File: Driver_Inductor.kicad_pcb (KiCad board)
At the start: 6 copper layers, 120.6 x 69.9 mm, 84 parts, among them J1 Control_A, J2 DC+, J3 DC-, J4 OUT1, J5 OUT2, U2 R-785.0-1.0, U3 LM1117GS-3.3, U4 LMV7219M5, U5 ADuM1200AR, U6 74LVC1G04

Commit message: Развел все дорожки
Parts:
- removed D15, D16: WRA1215S-3WR2, Mornsun:WRA1215S-3WR2
- removed R32, R33: 0, Resistor_SMD:R_0805_2012Metric_Pad1.20x1.40mm_HandSolder
- removed U2: R-785.0-1.0, Converter_DCDC:Converter_DCDC_RECOM_R-78E-0.5_THT
- added C10: 1u, Capacitor_THT:C_Rect_L31.5mm_W13.0mm_P27.50mm_MKS4, F.Cu at (87.0, 83.2)
- added C9: 2.2u, Capacitor_SMD:C_0805_2012Metric_Pad1.18x1.45mm_HandSolder, B.Cu at (132.7, 87.6)
- added D11: WRA1215S-3WR2, Mornsun:WRA_S-3WR2, F.Cu at (151.5, 99.1)
- added D12: K78xxM-1000R3, Mornsun:K78xx-1000R3, F.Cu at (177.8, 109.7)
- added D6: SN74AHC1G08DBVR, Package_TO_SOT_SMD:SOT-23-5, F.Cu at (126.7, 83.3)
- added D8: WRA1215S-3WR2, Mornsun:WRA_S-3WR2, F.Cu at (118.5, 99.1)
- C1, C17, C18, C2, C20, C22, C23, C24, C25, C26, C28, C3, C30, C33, C37, C4, D17, R14, R31, U6: moved to F.Cu
- C15, C8: moved to B.Cu
- J2, J3, J4, J5: footprint Connector_Power:M5 -> Connector_My:Bush_M4
- moved C30 102.9 mm to (158.1, 106.4), turned to 0 degrees
- moved J4 93.4 mm to (120.0, 68.0)
- moved C17 73.4 mm to (152.4, 85.1), turned to 90 degrees
- moved C16 69.8 mm to (166.5, 75.0), turned to 180 degrees
- moved C18 66.7 mm to (119.4, 85.1), turned to 90 degrees
- moved J5 64.8 mm to (139.5, 68.0)
- moved C31 62.5 mm to (173.5, 68.0), turned to -90 degrees
- moved C34 61.5 mm to (183.5, 71.5)
- moved C35 61.5 mm to (183.5, 76.5)
- moved C33 58.4 mm to (176.5, 68.0), turned to 90 degrees
- moved C24 50.1 mm to (124.5, 108.0), turned to 0 degrees
- moved C23 49.7 mm to (129.5, 108.0)
- moved C36 48.5 mm to (189.0, 76.5), turned to 180 degrees
- moved C26 45.4 mm to (135.9, 108.0)
- moved C25 45.4 mm to (141.0, 108.0), turned to 180 degrees
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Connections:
- net DESAT_H renamed DC+
- net Net-(J3-Pin_1) renamed DC-
- C23 pad 1: +15V_L1 -> -15V_L
- C24 pad 2: -15V_L1 -> +15V_L
- C25 pad 1: +15V_H1 -> -15V_H
- C26 pad 2: -15V_H1 -> +15V_H
- C30 pad 1: E2 -> E3
- C30 pad 2: -15V_L1 -> -15V_H
- C31 pad 2: -15V_L1 -> -15V_H
- C32 pad 2: -15V_L1 -> -15V_H
- C34 pad 2: -15V_L1 -> -15V_H
- D1 pad 13: +15V_L1 -> +15V_L
- D1 pad 16: -15V_L1 -> -15V_L
- D1 pad 9: -15V_L1 -> -15V_L
- D17 pad 1: OUT2 -> OUT2_Sens
- D17 pad 2: OUT2 -> OUT2_Sens
- D17 pad 3: OUT2 -> OUT2_Sens
- D17 pad 4: OUT2 -> OUT2_Sens
- D17 pad 5: OUT2_Sens -> OUT2
- D17 pad 6: OUT2_Sens -> OUT2
- D17 pad 7: OUT2_Sens -> OUT2
- D17 pad 8: OUT2_Sens -> OUT2
- D2 pad 13: +15V_H1 -> +15V_H
- D2 pad 16: -15V_H1 -> -15V_H
- D2 pad 9: -15V_H1 -> -15V_H
- J1 pad 1: unconnected-(J1-Pin_1-Pad1) -> Temp_N
- J1 pad 10: unconnected-(J1-Pin_10-Pad10) -> Fault_N
- J1 pad 11: unconnected-(J1-Pin_11-Pad11) -> PWM2_N
- J1 pad 12: unconnected-(J1-Pin_12-Pad12) -> Current
- J1 pad 2: unconnected-(J1-Pin_2-Pad2) -> +15V
- J1 pad 3: unconnected-(J1-Pin_3-Pad3) -> PWM1_P
- J1 pad 4: unconnected-(J1-Pin_4-Pad4) -> Fault_P
- J1 pad 5: unconnected-(J1-Pin_5-Pad5) -> PWM2_P
- J1 pad 6: unconnected-(J1-Pin_6-Pad6) -> Reset
- J1 pad 7: unconnected-(J1-Pin_7-Pad7) -> Temp_P
- J1 pad 8: unconnected-(J1-Pin_8-Pad8) -> GND
- J1 pad 9: unconnected-(J1-Pin_9-Pad9) -> PWM1_N
- R13 pad 2: unconnected-(R13-Pad2) -> +5V
- R26 pad 1: -15V_L1 -> -15V_H
- U3 pad 1: -15V_L1 -> -15V_H
- U3 pad 3: E2 -> E3
- U4 pad 2: -15V_L1 -> -15V_H
- U5 pad 4: -15V_L1 -> -15V_H
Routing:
- net RDY: track 0.04 -> 54.0 mm, vias 0 -> 5
- net FLT: track 1.02 -> 54.3 mm, vias 0 -> 4
- net Net-(D14-DI): track 0.00 -> 53.0 mm, vias 0 -> 2
- net PWM2_N: track 0.00 -> 48.9 mm, vias 0 -> 1
- net PWM2_P: track 0.00 -> 45.2 mm, vias 0 -> 1
- net Net-(D1-DESAT): track 0.00 -> 45.1 mm, vias 0 -> 2
- net PWM1_N: track 0.00 -> 42.6 mm, vias 0 -> 1
- net +5V: track 0.00 -> 41.6 mm, vias 0 -> 12
- net PWM1_P: track 0.00 -> 38.7 mm, vias 0 -> 1
- net Net-(D2-DESAT): track 0.00 -> 32.7 mm, vias 0 -> 2
- net Reset: track 0.00 -> 31.8 mm, vias 0 -> 1
- net GND: track 0.00 -> 28.3 mm, vias 1 -> 21
- net Current: track 0.09 -> 25.4 mm
- net Temp_N: track 0.00 -> 24.8 mm
- net Temp_P: track 0.00 -> 20.6 mm
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- added copper zone on F.Cu, net +15V
- added copper zone on In4.Cu, net +15V
- added copper zone on In3.Cu, net +15V_H
- added copper zone on In3.Cu, net +15V_L
- added copper zone on F.Cu, net +5V
- added copper zone on In2.Cu, net +5V
- added copper zone on In3.Cu, net +5V
- added copper zone on F.Cu, net +5VP
- added copper zone on In2.Cu, net +5VP
- added copper zone on F.Cu, net -15V_H
- added copper zone on In1.Cu, net -15V_H
- added copper zone on In4.Cu, net -15V_H
- added copper zone on In4.Cu, net -15V_L
- added copper zone on B.Cu, net DC+
- added copper zone on F.Cu, net DC+
- added copper zone on In1.Cu, net DC+
- added copper zone on In2.Cu, net DC+
- added copper zone on In3.Cu, net DC+
- added copper zone on In4.Cu, net DC+
- added copper zone on B.Cu, net DC-
- added copper zone on F.Cu, net DC-
- added copper zone on In1.Cu, net DC-
- added copper zone on In2.Cu, net DC-
- added copper zone on In3.Cu, net DC-
- added copper zone on In4.Cu, net DC-
- added copper zone on B.Cu, net E2
- added copper zone on B.Cu, net E3
- added copper zone on F.Cu, net E3
- added copper zone on F.Cu, net G2
- added copper zone on F.Cu, net G3
- added copper zone on B.Cu, net GND
- added copper zone on F.Cu, net GND
- added copper zone on F.Cu, net Net-(D1-Vout_off)
- added copper zone on F.Cu, net Net-(D1-Vout_on)
- added copper zone on F.Cu, net Net-(D2-Vout_off)
- added copper zone on F.Cu, net Net-(D2-Vout_on)
- added copper zone on B.Cu, net OUT1
- added copper zone on F.Cu, net OUT1
- added copper zone on In1.Cu, net OUT1
- added copper zone on In2.Cu, net OUT1
- added copper zone on In3.Cu, net OUT1
- added copper zone on In4.Cu, net OUT1
- added copper zone on B.Cu, net OUT2
- added copper zone on F.Cu, net OUT2
- added copper zone on In1.Cu, net OUT2
- added copper zone on In2.Cu, net OUT2
- added copper zone on In3.Cu, net OUT2
- added copper zone on In4.Cu, net OUT2
- added copper zone on B.Cu, net OUT2_Sens
- added copper zone on F.Cu, net OUT2_Sens
- added copper zone on In1.Cu, net OUT2_Sens
- added copper zone on In2.Cu, net OUT2_Sens
- added copper zone on In3.Cu, net OUT2_Sens
- added copper zone on In4.Cu, net OUT2_Sens
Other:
- board size 120.6 x 69.9 mm -> 119.6 x 60.5 mm
- board text removed: "Driver GD50FFY120C5S VER1.0.TEST"

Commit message: Заменил в схеме символы питания
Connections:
- net DC+ renamed DESAT_H
- net DC- renamed -VDC
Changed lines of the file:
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@@
 	(net 50 "unconnected-(D20-DC--Pad13)")
 	(net 51 "unconnected-(D20-DC--Pad14)")
-	(net 52 "DC+")
+	(net 52 "-VDC")
 	(net 53 "OUT1")
 	(net 54 "unconnected-(D20-DC+-Pad15)")
@@
 	(net 56 "unconnected-(D20-OUT3-Pad19)")
 	(net 57 "unconnected-(D20-OUT3-Pad20)")
-	(net 58 "DC-")
+	(net 58 "DESAT_H")
 	(net 59 "unconnected-(U5-VOB-Pad6)")
 	(net 60 "unconnected-(U5-VIB-Pad3)")
@@
 		)
 		(fp_text user "${REFERENCE}"
-			(at 0 0 360)
+			(at 0 0 0)
 			(layer "F.Fab")
 			(effects
@@
 		)
 		(property "Value" "120"
-			(at 0 1.65 360)
+			(at 0 1.65 0)
 			(layer "F.Fab")
 			(effects
@@
 		)
 		(property "Footprint" "Resistor_SMD:R_0805_2012Metric_Pad1.20x1.40mm_HandSolder"
-			(at 0 0 360)
+			(at 0 0 0)
 			(layer "F.Fab")
 			(hide yes)
@@
 		)
 		(property "Datasheet" ""
-			(at 0 0 360)
+			(at 0 0 0)
 			(layer "F.Fab")
 			(hide yes)
@@
 		)
 		(property "Description" ""
-			(at 0 0 360)
+			(at 0 0 0)
 			(layer "F.Fab")
 			(hide yes)
@@
 		)
 		(fp_text user "${REFERENCE}"
-			(at 0 0 360)
+			(at 0 0 0)
 			(layer "F.Fab")
 			(effects
@@
 		(tags "SOIC SO")
 		(property "Reference" "D17"
-			(at 3 -6 360)
+			(at 3 -6 0)
 			(layer "F.SilkS")
 			(effects
@@
 		)
 		(property "Value" "NSM2011-50B5R-DSWR"
-			(at 0 6.1 360)
+			(at 0 6.1 0)
 			(layer "F.Fab")
 			(effects
@@
 		)
 		(property "Footprint" "Package_SO:SOIC-16W_7.5x10.3mm_P1.27mm"
-			(at 0 0 360)
+			(at 0 0 0)
 			(layer "B.Fab")
 			(hide yes)
@@
 		)
 		(property "Datasheet" ""
-			(at 0 0 360)
+			(at 0 0 0)
 			(layer "B.Fab")
 			(hide yes)
@@
 		)
 		(property "Description" ""
-			(at 0 0 360)
+			(at 0 0 0)
 			(layer "B.Fab")
 			(hide yes)
@@
 		)
 		(fp_text user "${REFERENCE}"
-			(at 0 0 360)
+			(at 0 0 0)
 			(layer "F.Fab")
 			(effects
@@
 			(layers "*.Cu" "*.Mask")
 			(remove_unused_layers no)
-			(net 52 "DC+")
+			(net 58 "DESAT_H")
 			(pintype "passive")
 		)
@@
 			(layers "*.Cu" "*.Mask")
 			(remove_unused_layers no)
-			(net 58 "DC-")
+			(net 52 "-VDC")
 			(pintype "passive")
 		)
@@
 		)
 		(property "Value" "10k"
-			(at 0 1.65 360)
+			(at 0 1.65 0)
 			(layer "F.Fab")
 			(effects
@@
 		)
 		(property "Footprint" "Resistor_SMD:R_0805_2012Metric_Pad1.20x1.40mm_HandSolder"
-			(at 0 0 360)
+			(at 0 0 0)
 			(layer "F.Fab")
 			(hide yes)
@@
 		)
 		(property "Datasheet" ""
-			(at 0 0 360)
+			(at 0 0 0)
 			(layer "F.Fab")
 			(hide yes)
@@
 		)
 		(property "Description" ""
-			(at 0 0 360)
+			(at 0 0 0)
 			(layer "F.Fab")
 			(hide yes)
@@
 		)
 		(fp_text user "${REFERENCE}"
-			(at 0 0 360)
+			(at 0 0 0)
 			(layer "F.Fab")
 			(effects
@@
 			(layers "F.Cu" "F.Paste" "F.Mask")
 			(roundrect_rratio 0.1388888889)
-			(net 52 "DC+")
+			(net 58 "DESAT_H")
 			(pinfunction "K")
 			(pintype "passive")
@@
 		(tags "capacitor handsolder")
 		(property "Reference" "C30"
-			(at 0 -1.68 360)
+			(at 0 -1.68 0)
 			(layer "F.SilkS")
 			(effects
@@
 		)
 		(property "Value" "2.2u"
-			(at 0 1.68 360)
+			(at 0 1.68 0)
 			(layer "F.Fab")
 			(effects
@@
 		)
 		(property "Footprint" "Capacitor_SMD:C_0805_2012Metric_Pad1.18x1.45mm_HandSolder"
-			(at 0 0 360)
+			(at 0 0 0)
 			(layer "B.Fab")
 			(hide yes)
@@
 		)
 		(property "Datasheet" ""
-			(at 0 0 360)
+			(at 0 0 0)
 			(layer "B.Fab")
 			(hide yes)
@@
 		)
 		(property "Description" ""
-			(at 0 0 360)
+			(at 0 0 0)
 			(layer "B.Fab")
 			(hide yes)
@@
 		)
 		(fp_text user "${REFERENCE}"
-			(at 0 0 360)
+			(at 0 0 0)
 			(layer "F.Fab")
 			(effects
@@
 			(layers "*.Cu" "*.Mask")
 			(remove_unused_layers no)
-			(net 52 "DC+")
+			(net 58 "DESAT_H")
 			(pinfunction "DC+")
 			(pintype "input")
@@
 			(layers "*.Cu" "*.Mask")
 			(remove_unused_layers no)
-			(net 52 "DC+")
+			(net 58 "DESAT_H")
 			(pinfunction "DC+")
 			(pintype "input")
@@
 			(layers "*.Cu" "*.Mask")
 			(remove_unused_layers no)
-			(net 58 "DC-")
+			(net 52 "-VDC")
 			(pinfunction "DC-")
 			(pintype "input")
@@
 			(layers "*.Cu" "*.Mask")
 			(remove_unused_layers no)
-			(net 58 "DC-")
+			(net 52 "-VDC")
 			(pinfunction "DC-")
 			(pintype "input")
@@
 			(layers "*.Cu" "*.Mask")
 			(remove_unused_layers no)
-			(net 52 "DC+")
+			(net 58 "DESAT_H")
 			(pinfunction "Pin_1")
 			(pintype "passive")
@@
 		(tags "connector Molex Micro-Fit_3.0 vertical")
 		(property "Reference" "J1"
-			(at 7.5 -3.67 360)
+			(at 7.5 -3.67 0)
 			(layer "F.SilkS")
 			(effects
@@
 		)
 		(property "Value" "Control_A"
-			(at 7.5 7.51 360)
+			(at 7.5 7.51 0)
 			(layer "F.Fab")
 			(effects
@@
 		)
 		(fp_text user "${REFERENCE}"
-			(at 7.5 4.2 360)
+			(at 7.5 4.2 0)
 			(layer "F.Fab")
 			(effects
@@
 			(layers "*.Cu" "*.Mask")
 			(remove_unused_layers no)
-			(net 58 "DC-")
+			(net 52 "-VDC")
 			(pinfunction "Pin_1")
 			(pintype "passive")
@@
 		(tags "capacitor handsolder")
 		(property "Reference" "C27"
-			(at 2.921 -0.254 360)
+			(at 2.921 -0.254 0)
 			(layer "B.SilkS")
 			(effects
@@
 	)
 	(segment
-		(start 107.315 91.525)
-		(end 105.452 89.662)
+		(start 117.974 76.74)
+		(end 118.382 76.332)
 		(width 0.5)
 		(layer "F.Cu")
-		(net 52)
+		(net 53)
 	)
 	(segment
-		(start 107.315 95.155)
-		(end 107.315 91.525)
+		(start 113.03 76.74)
+		(end 117.974 76.74)
 		(width 0.5)
 		(layer "F.Cu")
-		(net 52)
+		(net 53)
 	)
 	(segment
-		(start 117.974 76.74)
-		(end 118.382 76.332)
+		(start 107.315 91.525)
+		(end 105.452 89.662)
 		(width 0.5)
 		(layer "F.Cu")
-		(net 53)
+		(net 58)
 	)
 	(segment
-		(start 113.03 76.74)
-		(end 117.974 76.74)
+		(start 107.315 95.155)
+		(end 107.315 91.525)
 		(width 0.5)
 		(layer "F.Cu")
-		(net 53)
+		(net 58)
 	)
 	(segment
@@
 		(polygon
 			(pts
-				(xy 167.894 112.522) (xy 168.656 112.522) (xy 168.656 112.522) (xy 173.482 112.522) (xy 173.482 111.252)
-				(xy 177.038 111.252) (xy 177.038 115.062) (xy 167.894 115.062)
+				(xy 167.894 112.522) (xy 168.656 112.522) (xy 173.482 112.522) (xy 173.482 111.252) (xy 177.038 111.252)
+				(xy 177.038 115.062) (xy 167.894 115.062)
 			)
 		)
@@
 		(polygon
 			(pts
-				(xy 167.894 107.95) (xy 167.894 107.95) (xy 167.894 107.442) (xy 172.974 107.442) (xy 172.974 108.458)
-				(xy 177.038 108.458) (xy 177.038 110.998) (xy 172.974 110.998) (xy 172.974 112.268) (xy 167.894 112.268)
-				(xy 167.894 111.506) (xy 167.894 111.506)
+				(xy 167.894 107.95) (xy 167.894 107.442) (xy 172.974 107.442) (xy 172.974 108.458) (xy 177.038 108.458)
+				(xy 177.038 110.998) (xy 172.974 110.998) (xy 172.974 112.268) (xy 167.894 112.268) (xy 167.894 111.506)
 			)
 		)
@@
 	)
 	(zone
-		(net 58)
-		(net_name "DC-")
+		(net 52)
+		(net_name "-VDC")
 		(layers "F.Cu" "In1.Cu" "In2.Cu" "In3.Cu" "In4.Cu" "B.Cu")
 		(hatch edge 0.5)
@@
 	)
 	(zone
-		(net 52)
-		(net_name "DC+")
+		(net 58)
+		(net_name "DESAT_H")
 		(layers "F.Cu" "In1.Cu" "In2.Cu" "In3.Cu" "In4.Cu" "B.Cu")
 		(hatch edge 0.5)
@@
 		(polygon
 			(pts
-				(xy 161.544 104.394) (xy 153.67 104.394) (xy 153.67 104.394) (xy 132.842 104.394) (xy 132.842 110.49)
-				(xy 161.544 110.49)
+				(xy 161.544 104.394) (xy 153.67 104.394) (xy 132.842 104.394) (xy 132.842 110.49) (xy 161.544 110.49)
 			)
 		)
@@
 		(polygon
 			(pts
-				(xy 132.842 104.394) (xy 153.67 104.394) (xy 153.67 104.394) (xy 155.956 104.394) (xy 155.956 110.744)
-				(xy 152.908 110.744) (xy 152.908 119.888) (xy 132.842 119.888)
+				(xy 132.842 104.394) (xy 153.67 104.394) (xy 155.956 104.394) (xy 155.956 110.744) (xy 152.908 110.744)
+				(xy 152.908 119.888) (xy 132.842 119.888)
 			)
 		)

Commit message: VER2.0 Отправил в резонит
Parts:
- removed C37: 56p, Capacitor_SMD:C_0805_2012Metric_Pad1.18x1.45mm_HandSolder
- removed C9: 2.2u, Capacitor_SMD:C_0805_2012Metric_Pad1.18x1.45mm_HandSolder
- removed R30: 120, Resistor_SMD:R_0805_2012Metric_Pad1.20x1.40mm_HandSolder
- removed R31: 10k, Resistor_SMD:R_0805_2012Metric_Pad1.20x1.40mm_HandSolder
- removed U6: 74LVC1G04, Package_TO_SOT_SMD:SOT-23-5_HandSoldering
- added G***: LOGO, Logo:Logo_EV_Tech, F.Cu at (90.6, 67.2)
- added G***: LOGO, Logo:Logo_Megawatt, F.Cu at (192.0, 111.6)
- added Q1: IRLML2402TRPBF, Package_TO_SOT_SMD:SOT-23, F.Cu at (132.8, 83.2)
- added R24: 0, Resistor_SMD:R_0805_2012Metric_Pad1.20x1.40mm_HandSolder, F.Cu at (132.8, 80.4)
- added R32: 1k, Resistor_SMD:R_0805_2012Metric_Pad1.20x1.40mm_HandSolder, F.Cu at (132.8, 86.0)
- D1, D2: value ADUM4135 -> NSI6651ASC-DSWR
- turned D1 to 90 degrees
- turned D2 to 90 degrees
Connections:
- C3 pad 2: Net-(D1-~{RESET}) -> Net-(D1-~{RST})
- C4 pad 2: Net-(D2-~{RESET}) -> Net-(D2-~{RST})
- D1 pad 1: GND -> -15V_L
- D1 pad 10: Net-(D1-DESAT) -> PWM2_P
- D1 pad 11: E2 -> PWM2_N
- D1 pad 12: Net-(D1-Vout_off) -> RDY
- D1 pad 13: +15V_L -> FLT
- D1 pad 14: Net-(D1-Vout_on) -> Net-(D1-~{RST})
- D1 pad 15: G2 -> +5V
- D1 pad 16: -15V_L -> GND
- D1 pad 2: PWM2_P -> Net-(D1-DESAT)
- D1 pad 3: PWM2_N -> E2
- D1 pad 4: RDY -> Net-(D1-OUTH)
- D1 pad 5: FLT -> +15V_L
- D1 pad 6: Net-(D1-~{RESET}) -> Net-(D1-OUTL)
- D1 pad 7: +5V -> G2
- D1 pad 8: GND -> -15V_L
- D1 pad 9: -15V_L -> GND
- D2 pad 1: GND -> -15V_H
- D2 pad 10: Net-(D2-DESAT) -> PWM1_P
- D2 pad 11: E3 -> PWM1_N
- D2 pad 12: Net-(D2-Vout_off) -> RDY
- D2 pad 13: +15V_H -> FLT
- D2 pad 14: Net-(D2-Vout_on) -> Net-(D2-~{RST})
- D2 pad 15: G3 -> +5V
- D2 pad 16: -15V_H -> GND
- D2 pad 2: PWM1_P -> Net-(D2-DESAT)
- D2 pad 3: PWM1_N -> E3
- D2 pad 4: RDY -> Net-(D2-OUTH)
- D2 pad 5: FLT -> +15V_H
- D2 pad 6: Net-(D2-~{RESET}) -> Net-(D2-OUTL)
- D2 pad 7: +5V -> G3
- D2 pad 8: GND -> -15V_H
- D2 pad 9: -15V_H -> GND
- R1 pad 2: Net-(D1-~{RESET}) -> Net-(D1-~{RST})
- R15 pad 2: Net-(D1-Vout_on) -> Net-(D1-OUTL)
- R16 pad 2: Net-(D1-Vout_on) -> Net-(D1-OUTL)
- R17 pad 2: Net-(D1-Vout_off) -> Net-(D1-OUTH)
- R18 pad 2: Net-(D1-Vout_off) -> Net-(D1-OUTH)
- R19 pad 2: Net-(D2-Vout_on) -> Net-(D2-OUTL)
- R2 pad 2: Net-(D2-~{RESET}) -> Net-(D2-~{RST})
- R20 pad 2: Net-(D2-Vout_off) -> Net-(D2-OUTH)
- R21 pad 2: Net-(D2-Vout_off) -> Net-(D2-OUTH)
- R22 pad 2: Net-(D2-Vout_off) -> Net-(D2-OUTH)
- R3 pad 2: Net-(D1-Vout_on) -> Net-(D1-OUTL)
- R4 pad 2: Net-(D1-Vout_off) -> Net-(D1-OUTH)
- R5 pad 2: Net-(D2-Vout_on) -> Net-(D2-OUTL)
- R6 pad 2: Net-(D2-Vout_on) -> Net-(D2-OUTL)
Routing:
- net Net-(C37-Pad1): track 7.17 -> 0.00 mm
- net Net-(D2-~{RST}): track 0.00 -> 6.28 mm
- net Net-(D2-~{RESET}): track 6.28 -> 0.00 mm
- net Net-(D1-~{RST}): track 0.00 -> 6.28 mm
- net Net-(D1-~{RESET}): track 6.28 -> 0.00 mm
- net RST: track 12.7 -> 17.0 mm
- net Net-(Q1-G): track 0.00 -> 1.88 mm
- net +5V: track 41.6 -> 40.0 mm
- net GND: track 28.3 -> 29.1 mm, vias 21 -> 18
- added copper zone on F.Cu, net Net-(D1-OUTH)
- added copper zone on F.Cu, net Net-(D1-OUTL)
- added copper zone on F.Cu, net Net-(D2-OUTH)
- added copper zone on F.Cu, net Net-(D2-OUTL)
- removed copper zone on F.Cu, net Net-(D1-Vout_off)
- removed copper zone on F.Cu, net Net-(D1-Vout_on)
- removed copper zone on F.Cu, net Net-(D2-Vout_off)
- removed copper zone on F.Cu, net Net-(D2-Vout_on)
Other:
- board text added: "Driver board VER2.0"

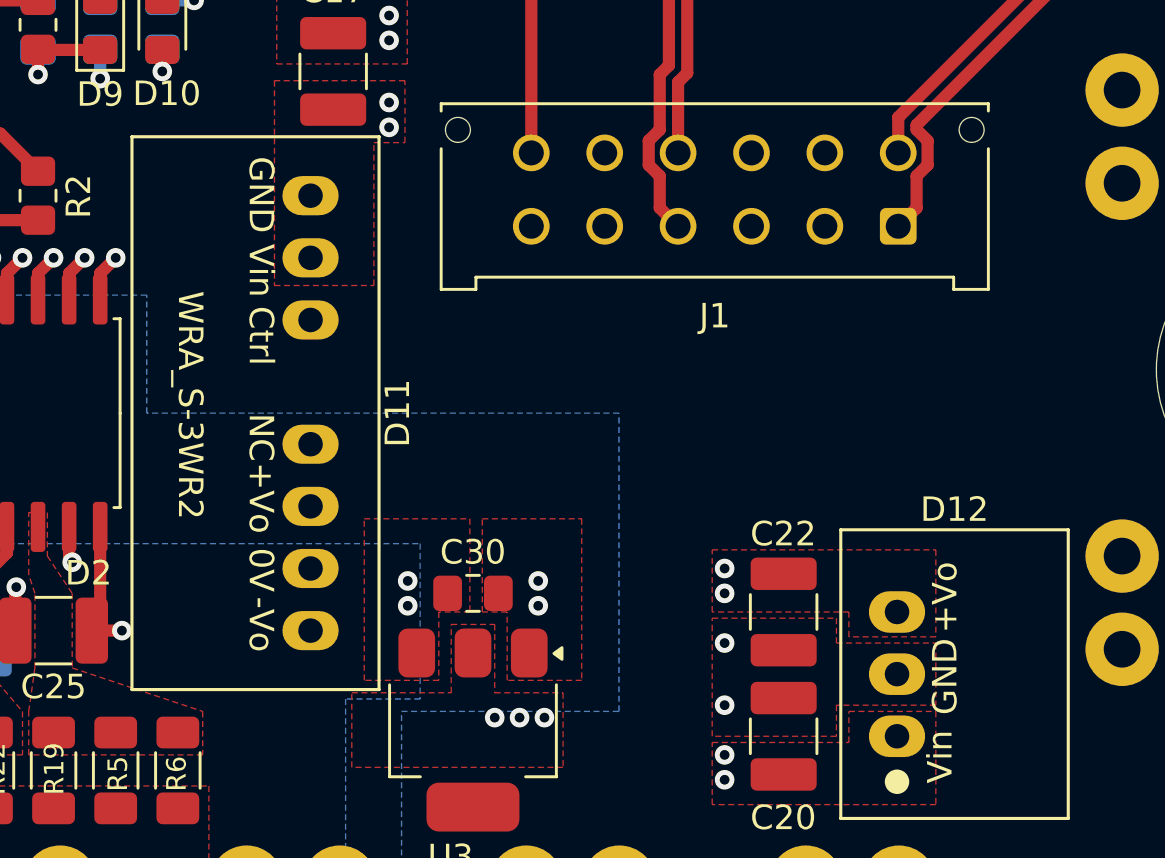
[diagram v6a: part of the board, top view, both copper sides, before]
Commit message: Изменения: добавил 5 вольтовые RS485 на вход драйверов
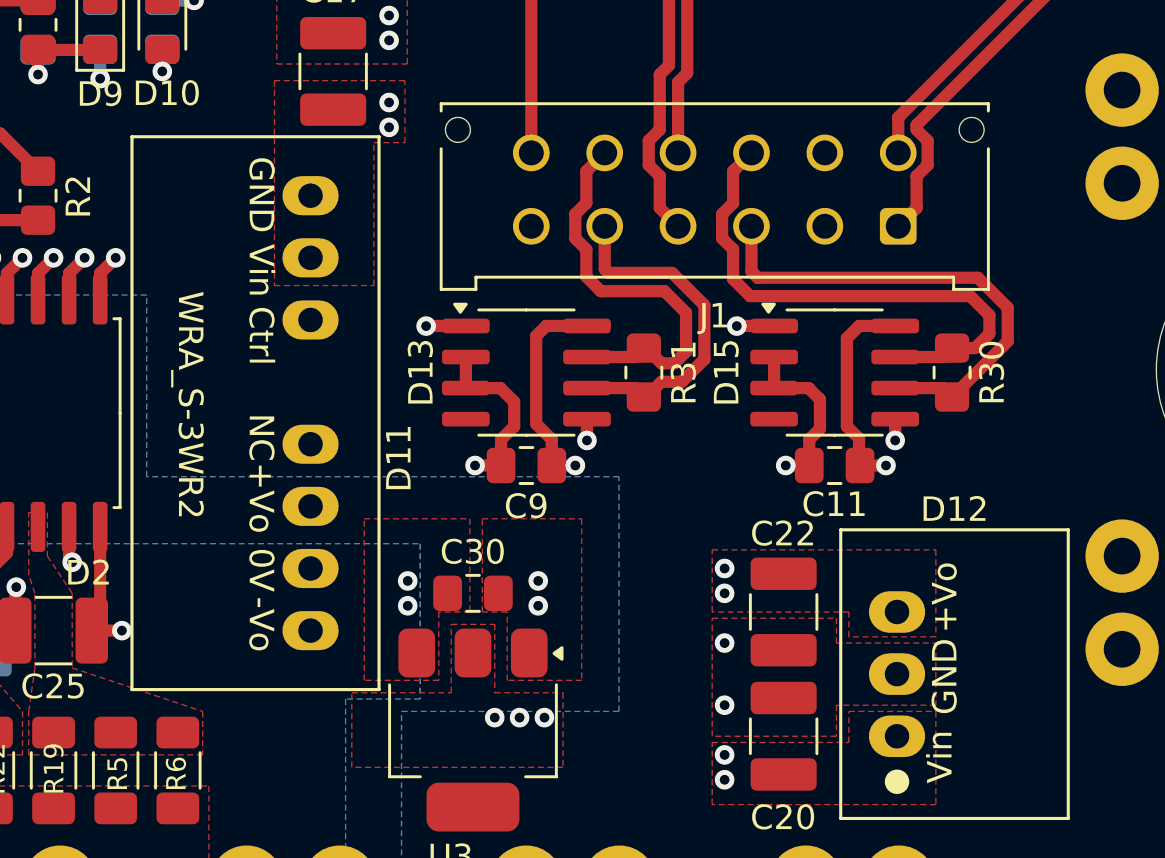
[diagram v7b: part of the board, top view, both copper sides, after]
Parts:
- added C11: 2.2u, Capacitor_SMD:C_0805_2012Metric_Pad1.18x1.45mm_HandSolder, F.Cu at (172.9, 101.2)
- added C9: 2.2u, Capacitor_SMD:C_0805_2012Metric_Pad1.18x1.45mm_HandSolder, F.Cu at (160.3, 101.2)
- added D13: ADM1485JRZ, Package_SO:SOIC-8_3.9x4.9mm_P1.27mm, F.Cu at (160.3, 97.4)
- added D15: ADM1485JRZ, Package_SO:SOIC-8_3.9x4.9mm_P1.27mm, F.Cu at (172.9, 97.4)
- added R30: 120, Resistor_SMD:R_0805_2012Metric_Pad1.20x1.40mm_HandSolder, F.Cu at (177.7, 97.4)
- added R31: 120, Resistor_SMD:R_0805_2012Metric_Pad1.20x1.40mm_HandSolder, F.Cu at (165.1, 97.4)
- D5, D7: value MURS360T3G -> MURS160
- U3: value LM1117GS-3.3 -> LM1117GS-5.0
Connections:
- D1 pad 10: PWM2_P -> PWM2
- D1 pad 11: PWM2_N -> GND
- D2 pad 10: PWM1_P -> PWM1
- D2 pad 11: PWM1_N -> GND
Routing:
- net PWM2: track 0.00 -> 38.0 mm, vias 0 -> 2
- net PWM1: track 0.00 -> 36.7 mm, vias 0 -> 2
- net PWM2_N: track 48.9 -> 16.7 mm, vias 1 -> 0
- net PWM2_P: track 45.2 -> 14.2 mm, vias 1 -> 0
- net PWM1_N: track 42.6 -> 21.9 mm, vias 1 -> 0
- net GND: track 29.1 -> 49.3 mm, vias 18 -> 24
- net PWM1_P: track 38.7 -> 20.0 mm, vias 1 -> 0
- net +5V: track 40.0 -> 57.4 mm, vias 12 -> 14
